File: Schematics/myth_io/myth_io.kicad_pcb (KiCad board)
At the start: 2 copper layers, 28 parts, among them J1 Conn_01x08_Pin, J2 Conn_01x08_Pin, J3 Conn_01x08_Pin, J4 Conn_01x08_Pin, J5 Conn_02x01, J6 Conn_01x08_Pin, J7 Conn_01x16_Pin, J8 Conn_01x16_Pin, U1 74HC14, U10 74AHC574, U11 74AHC273, U12 74HC238, U13 74HC238, U14 74AHC138, U15 74AHC138, U2 74LS02, U3 74AHC04, U4 74HC74, U5 74HC163, U6 74HC238, U7 74HC595, U8 74HC165, U9 74AHC574, X1 CXO_DIP14

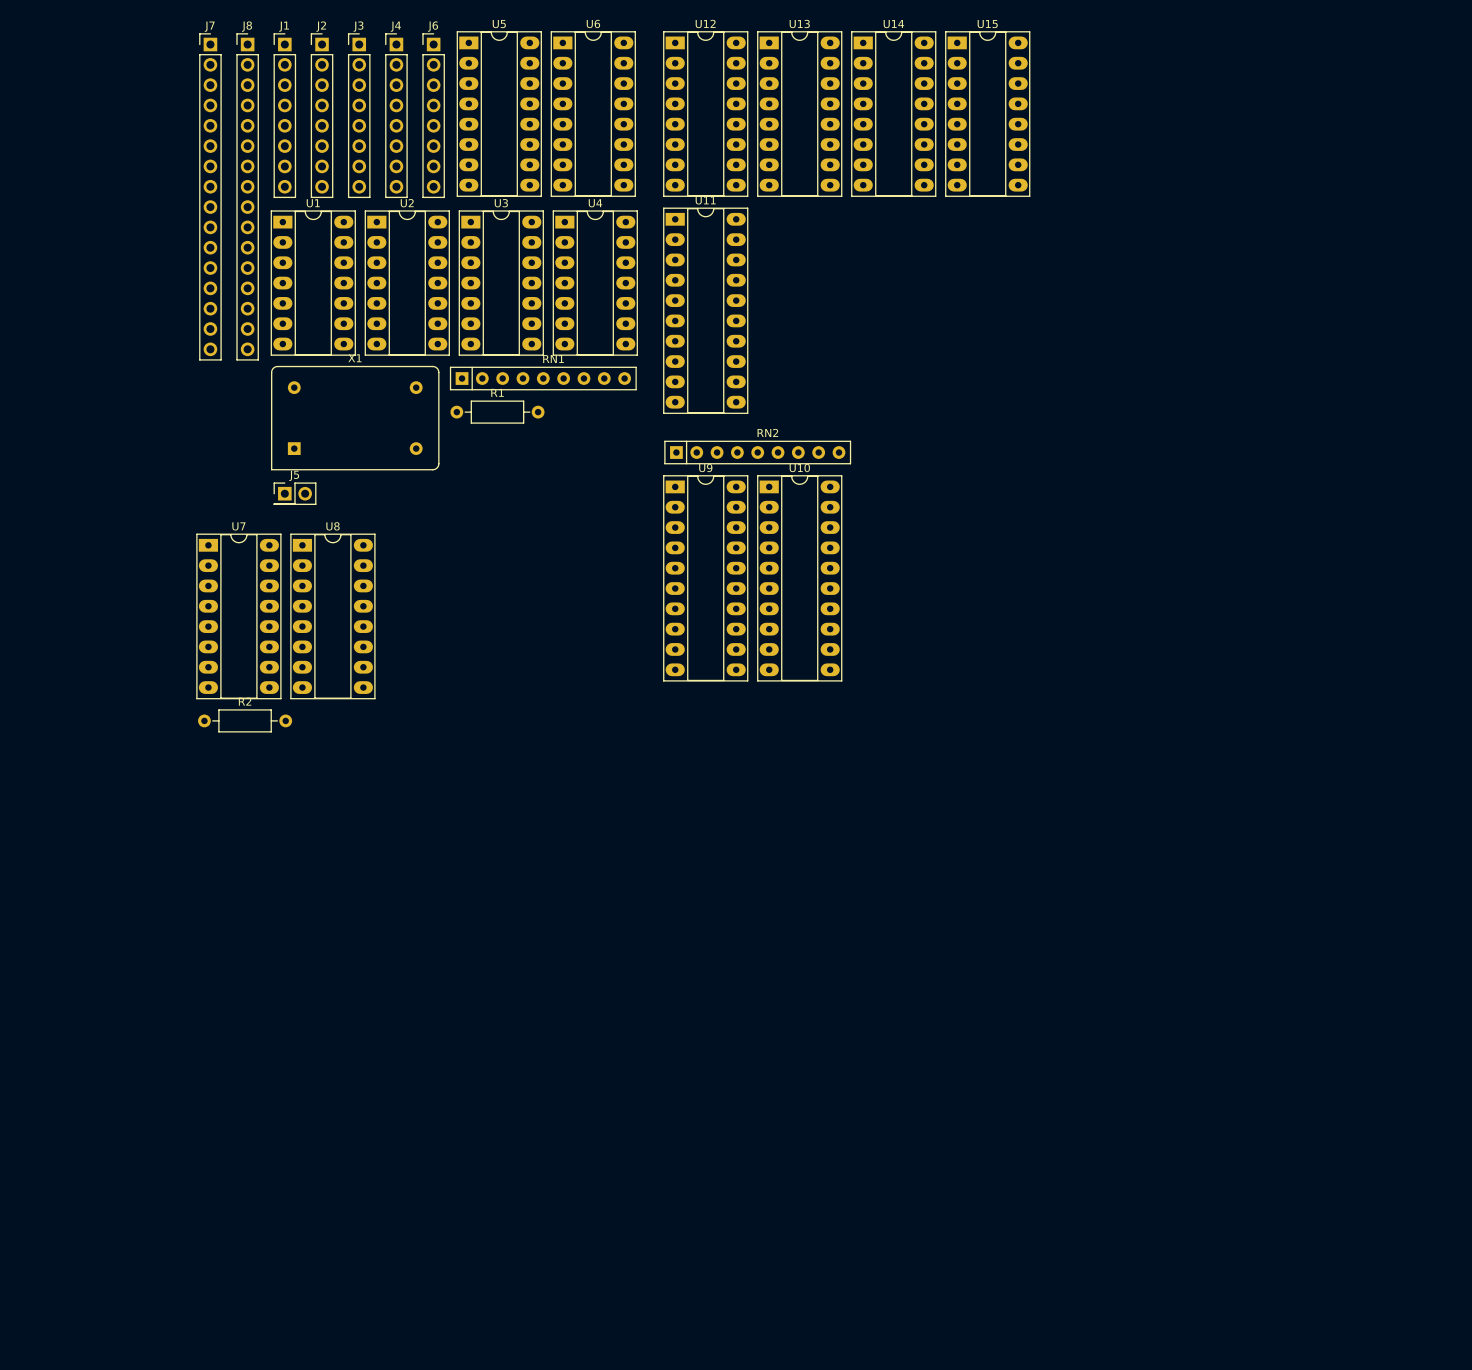
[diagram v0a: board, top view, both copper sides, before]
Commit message: Change d to g
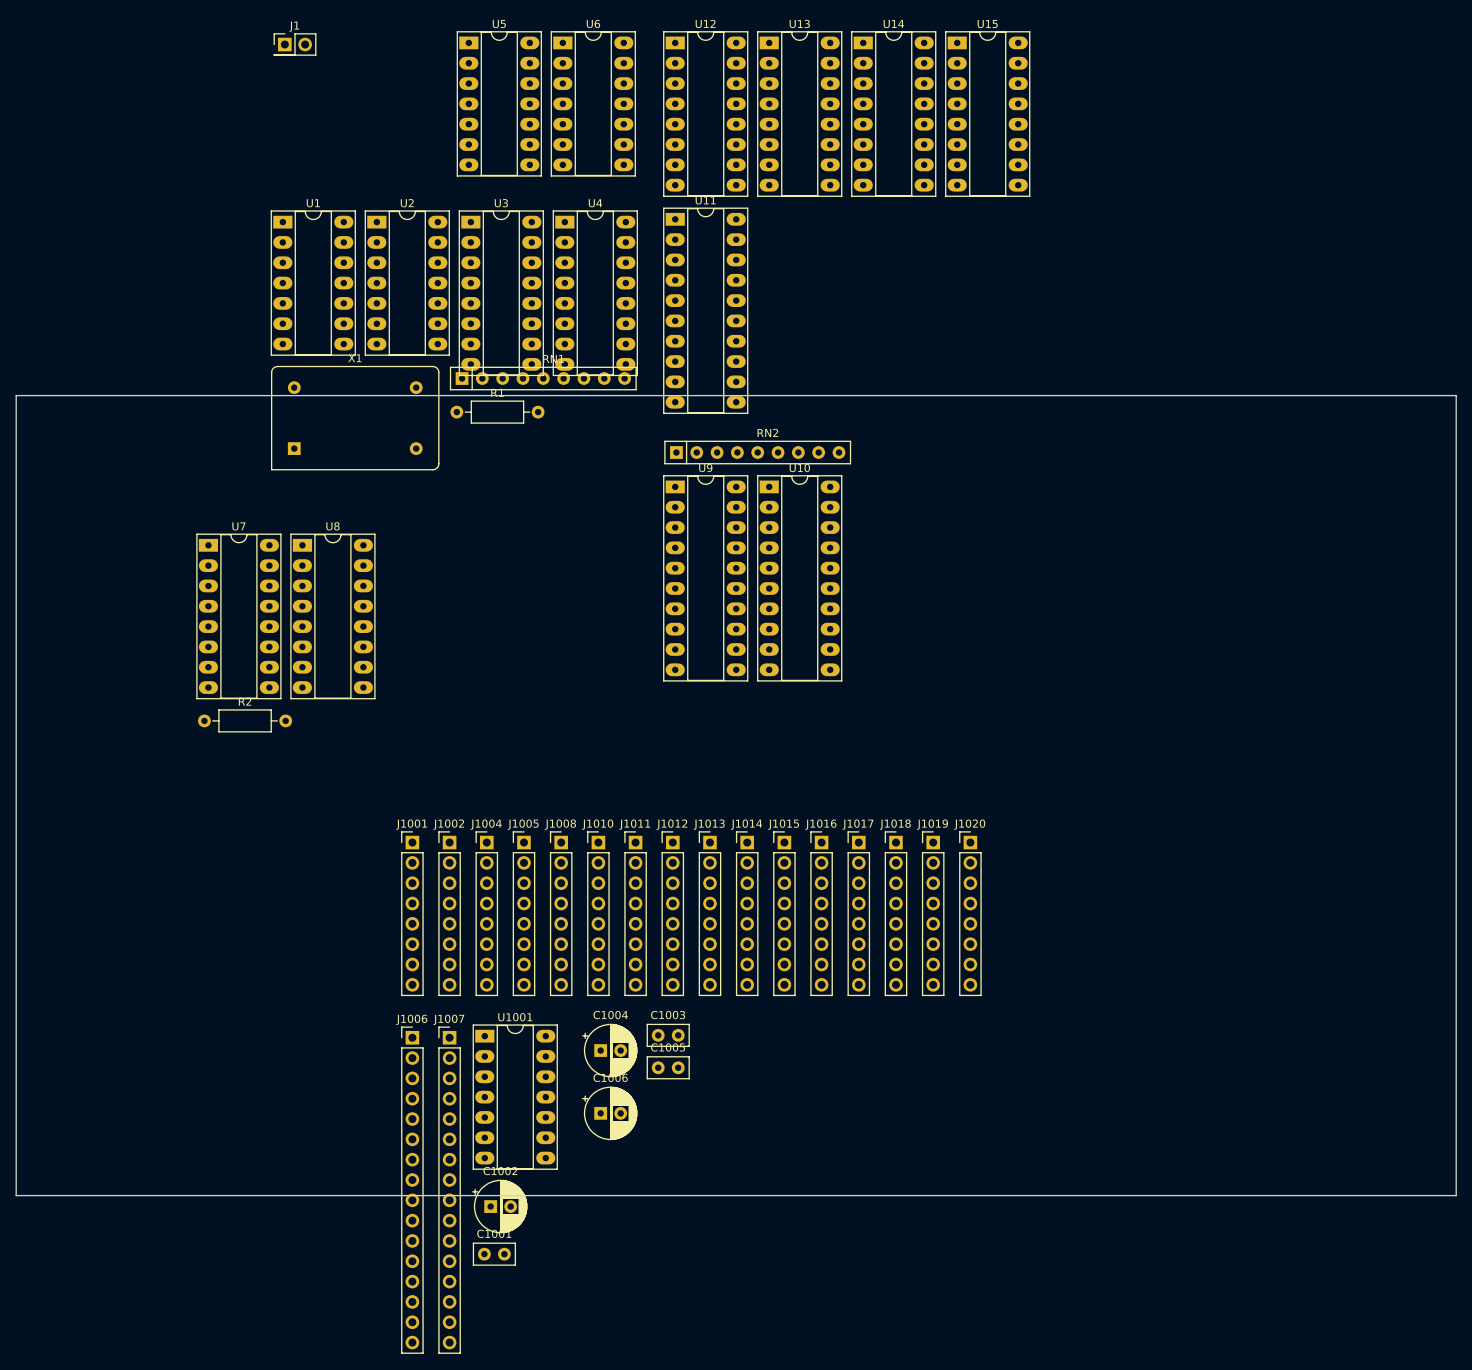
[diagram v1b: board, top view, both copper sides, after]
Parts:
- removed J2, J3, J4, J6: Conn_01x08_Pin, Connector_PinHeader_2.54mm:PinHeader_1x08_P2.54mm_Vertical
- removed J5: Conn_02x01, Connector_PinHeader_2.54mm:PinHeader_2x01_P2.54mm_Vertical
- removed J7, J8: Conn_01x16_Pin, Connector_PinHeader_2.54mm:PinHeader_1x16_P2.54mm_Vertical
- added C1001: C 100nF, Capacitor_THT:C_Disc_D5.0mm_W2.5mm_P2.50mm, F.Cu at (84.8, 153.1)
- added C1002: CP 10μF, Capacitor_THT:CP_Radial_D6.3mm_P2.50mm, F.Cu at (85.5, 147.1)
- added C1003: C 100nF, Capacitor_THT:C_Disc_D5.0mm_W2.5mm_P2.50mm, F.Cu at (106.5, 125.7)
- added C1004: CP 10μF, Capacitor_THT:CP_Radial_D6.3mm_P2.50mm, F.Cu at (99.3, 127.6)
- added C1005: C 100nF, Capacitor_THT:C_Disc_D5.0mm_W2.5mm_P2.50mm, F.Cu at (106.5, 129.8)
- added C1006: CP 10μF, Capacitor_THT:CP_Radial_D6.3mm_P2.50mm, F.Cu at (99.3, 135.5)
- added J1001: Conn_01x08_Pin, Connector_PinHeader_2.54mm:PinHeader_1x08_P2.54mm_Vertical, F.Cu at (75.8, 101.6)
- added J1002: Conn_01x08_Pin, Connector_PinHeader_2.54mm:PinHeader_1x08_P2.54mm_Vertical, F.Cu at (80.4, 101.6)
- added J1004: Conn_01x08_Pin, Connector_PinHeader_2.54mm:PinHeader_1x08_P2.54mm_Vertical, F.Cu at (85.0, 101.6)
- added J1005: Conn_01x08_Pin, Connector_PinHeader_2.54mm:PinHeader_1x08_P2.54mm_Vertical, F.Cu at (89.7, 101.6)
- added J1006: Conn_01x16_Pin, Connector_PinHeader_2.54mm:PinHeader_1x16_P2.54mm_Vertical, F.Cu at (75.8, 126.0)
- added J1007: Conn_01x16_Pin, Connector_PinHeader_2.54mm:PinHeader_1x16_P2.54mm_Vertical, F.Cu at (80.4, 126.0)
- added J1008: Conn_01x08_Pin, Connector_PinHeader_2.54mm:PinHeader_1x08_P2.54mm_Vertical, F.Cu at (94.3, 101.6)
- added J1010: Conn_01x08_Pin, Connector_PinHeader_2.54mm:PinHeader_1x08_P2.54mm_Vertical, F.Cu at (99.0, 101.6)
- added J1011: Conn_01x08_Pin, Connector_PinHeader_2.54mm:PinHeader_1x08_P2.54mm_Vertical, F.Cu at (103.7, 101.6)
- added J1012: Conn_01x08_Pin, Connector_PinHeader_2.54mm:PinHeader_1x08_P2.54mm_Vertical, F.Cu at (108.3, 101.6)
- added J1013: Conn_01x08_Pin, Connector_PinHeader_2.54mm:PinHeader_1x08_P2.54mm_Vertical, F.Cu at (113.0, 101.6)
- added J1014: Conn_01x08_Pin, Connector_PinHeader_2.54mm:PinHeader_1x08_P2.54mm_Vertical, F.Cu at (117.6, 101.6)
- added J1015: Conn_01x08_Pin, Connector_PinHeader_2.54mm:PinHeader_1x08_P2.54mm_Vertical, F.Cu at (122.2, 101.6)
- added J1016: Conn_01x08_Pin, Connector_PinHeader_2.54mm:PinHeader_1x08_P2.54mm_Vertical, F.Cu at (126.9, 101.6)
- added J1017: Conn_01x08_Pin, Connector_PinHeader_2.54mm:PinHeader_1x08_P2.54mm_Vertical, F.Cu at (131.6, 101.6)
- added J1018: Conn_01x08_Pin, Connector_PinHeader_2.54mm:PinHeader_1x08_P2.54mm_Vertical, F.Cu at (136.2, 101.6)
- added J1019: Conn_01x08_Pin, Connector_PinHeader_2.54mm:PinHeader_1x08_P2.54mm_Vertical, F.Cu at (140.8, 101.6)
- added J1020: Conn_01x08_Pin, Connector_PinHeader_2.54mm:PinHeader_1x08_P2.54mm_Vertical, F.Cu at (145.5, 101.6)
- added U1001: 74AHC04, Package_DIP:DIP-14_W7.62mm_Socket_LongPads, F.Cu at (84.8, 125.8)
- J1: value Conn_01x08_Pin -> Conn_02x01; footprint Connector_PinHeader_2.54mm:PinHeader_1x08_P2.54mm_Vertical -> Connector_PinHeader_2.54mm:PinHeader_2x01_P2.54mm_Vertical
- U3: value 74AHC04 -> 74HC163; footprint Package_DIP:DIP-14_W7.62mm_Socket_LongPads -> Package_DIP:DIP-16_W7.62mm_Socket_LongPads
- U4: value 74HC74 -> 74HC238; footprint Package_DIP:DIP-14_W7.62mm_Socket_LongPads -> Package_DIP:DIP-16_W7.62mm_Socket_LongPads
- U5: value 74HC163 -> 74AHC04; footprint Package_DIP:DIP-16_W7.62mm_Socket_LongPads -> Package_DIP:DIP-14_W7.62mm_Socket_LongPads
- U6: value 74HC238 -> 74HC74; footprint Package_DIP:DIP-16_W7.62mm_Socket_LongPads -> Package_DIP:DIP-14_W7.62mm_Socket_LongPads
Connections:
- net /Parallel IO/IO0 renamed IO0
- net /Parallel IO/IO1 renamed IO1
- net /Parallel IO/IO2 renamed IO2
- net /Parallel IO/IO3 renamed IO3
- net /Parallel IO/IO4 renamed IO4
- net /Parallel IO/IO5 renamed IO5
- net /Parallel IO/IO6 renamed IO6
- net /Parallel IO/IO7 renamed IO7
- net /SH1_PARLE renamed SH1_PARLE
- net /SSI renamed SSI
- net /~{SL1_PAROE} renamed ~{SL1_PAROE}
- J1 pad 1: +5V -> GND
- J1 pad 2: GND -> Net-(J1-Pin_2)
- R1 pad 1: Net-(J1-Pin_3) -> ~{RES_DIRTY}
- R2 pad 2: /MISO -> MISO
- U1 pad 1: /MISO -> MISO
- U1 pad 10: RES -> Net-(U1-Pad10)
- U1 pad 11: Net-(J1-Pin_3) -> ~{RES_DIRTY}
- U1 pad 13: RES -> Net-(U1-Pad10)
- U11 pad 11: /xE -> xE
- U12 pad 10: /Enable Register/SH5 -> SH5
- U12 pad 11: /Enable Register/SH4 -> SH4
- U12 pad 12: /Enable Register/SH3 -> SH3
- U12 pad 13: /Enable Register/SH2 -> SH2
- U12 pad 15: /SH0_NULL -> SH0_NULL
- U12 pad 7: /Enable Register/SH7 -> SH7
- U12 pad 9: /Enable Register/SH6 -> SH6
- U13 pad 10: /Enable Register/SH13 -> SH13
- U13 pad 11: /Enable Register/SH12 -> SH12
- U13 pad 12: /Enable Register/SH11 -> SH11
- U13 pad 13: /Enable Register/SH10 -> SH10
- U13 pad 14: /Enable Register/SH9 -> SH9
- U13 pad 15: /Enable Register/SH8 -> SH8
- U13 pad 7: /Enable Register/SH15 -> SH15
- U13 pad 9: /Enable Register/SH14 -> SH14
- U14 pad 10: /Enable Register/~{SL5} -> ~{SL5}
- U14 pad 11: /Enable Register/~{SL4} -> ~{SL4}
- U14 pad 12: /Enable Register/~{SL3} -> ~{SL3}
- U14 pad 13: /Enable Register/~{SL2} -> ~{SL2}
- U14 pad 15: /~{SL0_NULL} -> ~{SL0_NULL}
- U14 pad 7: /Enable Register/~{SL7} -> ~{SL7}
- U14 pad 9: /Enable Register/~{SL6} -> ~{SL6}
- U15 pad 10: /Enable Register/~{SL13} -> ~{SL13}
- U15 pad 11: /Enable Register/~{SL12} -> ~{SL12}
- U15 pad 12: /Enable Register/~{SL11} -> ~{SL11}
- U15 pad 13: /Enable Register/~{SL10} -> ~{SL10}
- U15 pad 14: /Enable Register/~{SL9} -> ~{SL9}
- U15 pad 15: /Enable Register/~{SL8} -> ~{SL8}
- U15 pad 7: /Enable Register/~{SL15} -> ~{SL15}
- U15 pad 9: /Enable Register/~{SL14} -> ~{SL14}
- U2 pad 1: Net-(U5-~{MR}) -> Net-(U3-~{MR})
- U2 pad 10: Net-(U4A-~{R}) -> Net-(U6A-~{R})
- U2 pad 8: /SCL -> SCL
- U3 pad 1: /SCH -> Net-(U3-~{MR})
- U3 pad 10: unconnected-(U3-Pad10) -> +5V
- U3 pad 11: GND -> CLOSE
- U3 pad 12: unconnected-(U3-Pad12) -> DPH
- U3 pad 13: GND -> Net-(U3-Q1)
- U3 pad 14: +5V -> Net-(U3-Q0)
- U3 pad 2: Net-(U4A-~{S}) -> Net-(J1-Pin_2)
- U3 pad 3: /xS -> GND
- U3 pad 4: Net-(U8-~{PL}) -> GND
- U3 pad 5: /Sx -> GND
- U3 pad 6: Net-(U7-~{OE}) -> GND
- U3 pad 7: GND -> +5V
- U3 pad 8: Net-(U10-OE) -> GND
- U3 pad 9: /Px -> +5V
- U4 pad 1: Net-(U4A-~{R}) -> Net-(U3-Q0)
- U4 pad 10: +5V -> unconnected-(U4-Y5-Pad10)
- U4 pad 11: GND -> PH2
- U4 pad 12: GND -> unconnected-(U4-Y3-Pad12)
- U4 pad 13: +5V -> PH1
- U4 pad 14: +5V -> unconnected-(U4-Y1-Pad14)
- U4 pad 2: +5V -> Net-(U3-Q1)
- U4 pad 3: GND -> DPH
- U4 pad 4: Net-(U4A-~{S}) -> CLOSE
- U4 pad 5: /SCLK -> GND
- U4 pad 6: unconnected-(U4A-~{Q}-Pad6) -> +5V
- U4 pad 7: GND -> unconnected-(U4-Y7-Pad7)
- U4 pad 8: unconnected-(U4B-~{Q}-Pad8) -> GND
- U4 pad 9: unconnected-(U4B-Q-Pad9) -> PH3
- U5 pad 1: Net-(U5-~{MR}) -> SCH
- U5 pad 10: +5V -> unconnected-(U5-Pad10)
- U5 pad 11: CLOSE -> GND
- U5 pad 12: DPH -> (no net)
- U5 pad 13: Net-(U5-Q1) -> (no net)
- U5 pad 14: Net-(U5-Q0) -> +5V
- U5 pad 2: Net-(J5-Pin_2) -> Net-(U6A-~{S})
- U5 pad 3: GND -> xS
- U5 pad 4: GND -> Net-(U8-~{PL})
- U5 pad 5: GND -> Sx
- U5 pad 6: GND -> Net-(U7-~{OE})
- U5 pad 7: +5V -> GND
- U5 pad 8: GND -> Net-(U10-OE)
- U5 pad 9: +5V -> Px
- U6 pad 1: Net-(U5-Q0) -> Net-(U6A-~{R})
- U6 pad 10: unconnected-(U6-Y5-Pad10) -> +5V
- U6 pad 11: PH2 -> GND
- U6 pad 12: unconnected-(U6-Y3-Pad12) -> GND
- U6 pad 13: PH1 -> +5V
- U6 pad 14: unconnected-(U6-Y1-Pad14) -> +5V
- U6 pad 2: Net-(U5-Q1) -> +5V
- U6 pad 3: DPH -> GND
- U6 pad 4: CLOSE -> Net-(U6A-~{S})
- U6 pad 5: GND -> SCLK
- U6 pad 6: +5V -> unconnected-(U6A-~{Q}-Pad6)
- U6 pad 7: unconnected-(U6-Y7-Pad7) -> GND
- U6 pad 8: GND -> unconnected-(U6B-~{Q}-Pad8)
- U6 pad 9: PH3 -> unconnected-(U6B-Q-Pad9)
- U8 pad 2: /SSO -> SSO
- U8 pad 9: /MOSI -> MOSI
- U9 pad 11: /xP -> xP
- X1 pad 8: Net-(J5-Pin_2) -> Net-(J1-Pin_2)
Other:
- board outline added: 180 x 100 mm
